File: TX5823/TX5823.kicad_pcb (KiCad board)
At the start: 2 copper layers, 84 parts, among them IC1 ATMEGA328P-A, IC2 ATTINY13A-SS, P1 Akku_in, P2 ISP, P3 Mavlink, U3 TPS7A7200RGT, U5 OPTO-TRANSISTOR4, U8 OPTO-TRANSISTOR4, Y1 16MHz

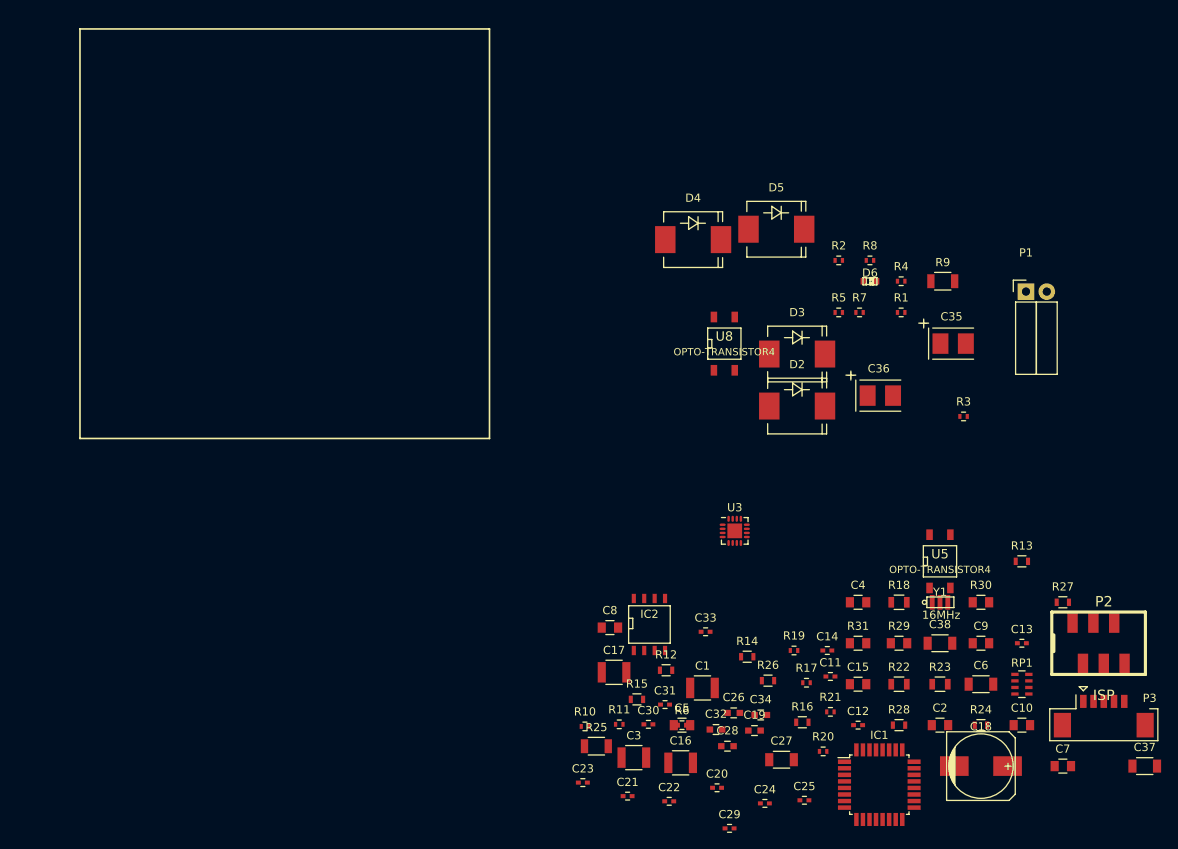
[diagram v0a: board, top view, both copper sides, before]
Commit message: weitere Footprints zugeordnet grobe Anordnung der Bauteiele im Layout
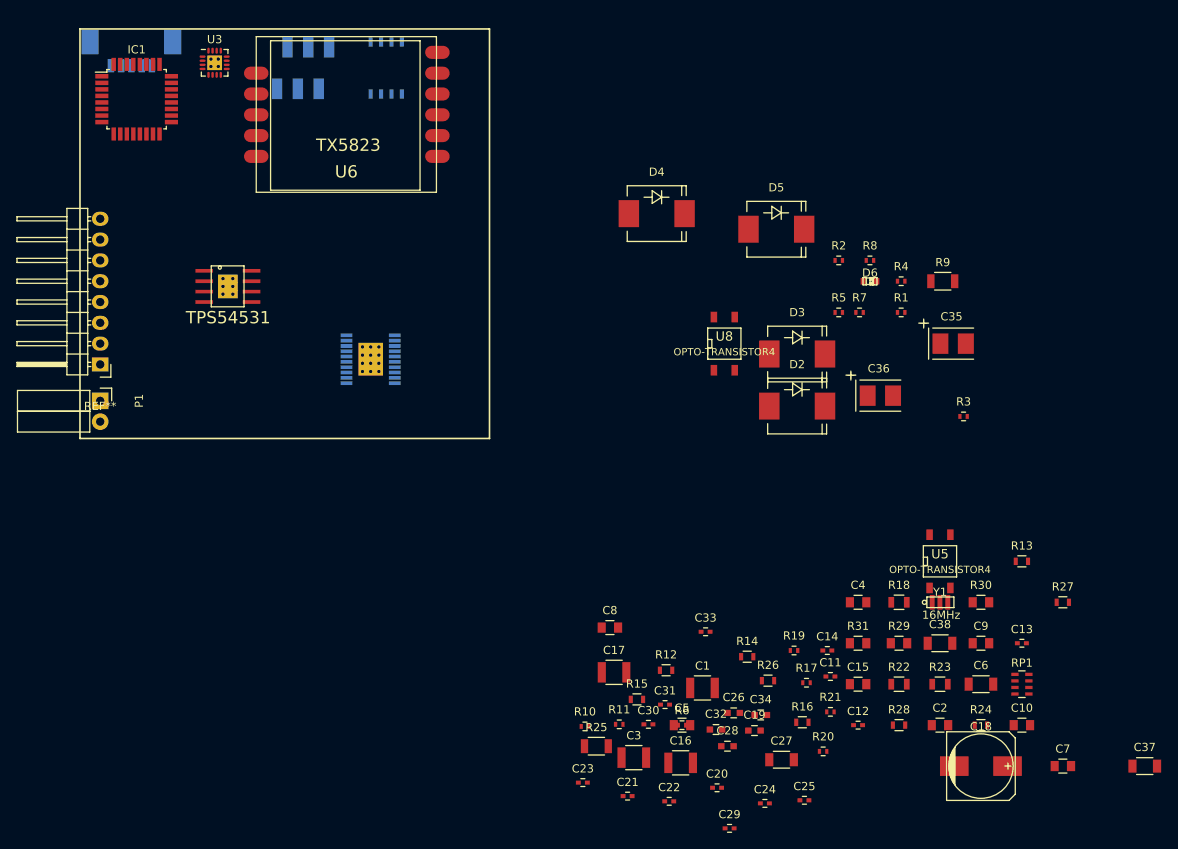
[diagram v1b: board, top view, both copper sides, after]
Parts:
- added REF**: Pin_Header_Angled_1x08, Pin_Headers:Pin_Header_Angled_1x08, F.Cu at (77.5, 61.0)
- added U1: LM25118, toni:TSSOP-20_4.4x6.5mm_Pitch0.65mm_EP, B.Cu at (110.5, 60.3)
- added U2: TPS54531, toni:SO8_EP, F.Cu at (90.2, 49.5)
- added U6: TX5823, toni:TX5823, F.Cu at (108.0, 30.5)
- IC2, P2, P3: moved to B.Cu
- U3: footprint Housings_DFN_QFN:QFN-16-1EP_3x3mm_Pitch0.5mm -> toni:QFN-16-1EP_3x3mm_Pitch0.5mm
- moved P3 145.1 mm to (81.3, 21.6)
- moved IC1 123.4 mm to (81.9, 28.6)
- moved P2 119.9 mm to (102.9, 24.8)
- moved P1 113.8 mm to (77.5, 65.4), turned to 270 degrees
- moved U3 85.4 mm to (91.4, 24.1)
- moved IC2 75.2 mm to (112.4, 24.8)
- moved D4 5.46 mm to (145.4, 42.5)
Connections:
- C11 pad 1: (no net) -> Net-(C11-Pad1)
- C12 pad 2: (no net) -> Net-(C12-Pad2)
- C13 pad 1: (no net) -> Net-(C13-Pad1)
- C14 pad 1: (no net) -> Net-(C14-Pad1)
- C14 pad 2: (no net) -> Net-(C14-Pad2)
- C15 pad 2: (no net) -> Net-(C15-Pad2)
- C2 pad 1: (no net) -> Net-(C2-Pad1)
- C4 pad 1: (no net) -> Net-(C4-Pad1)
- IC2 pad 5: (no net) -> Net-(IC2-Pad5)
- IC2 pad 7: (no net) -> Net-(IC2-Pad7)
- R3 pad 1: (no net) -> Net-(R3-Pad1)
- R4 pad 2: (no net) -> Net-(R4-Pad2)

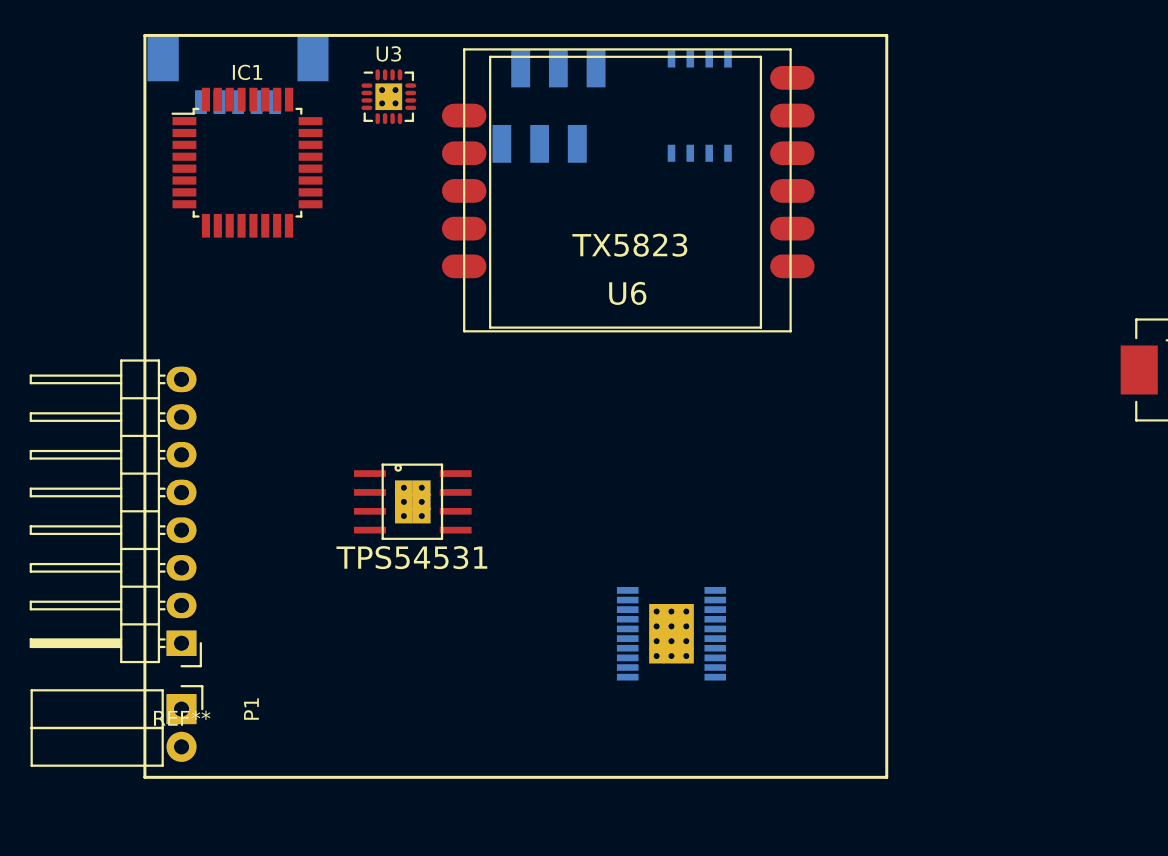
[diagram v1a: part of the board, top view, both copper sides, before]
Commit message: sma buchse hinzugefügt
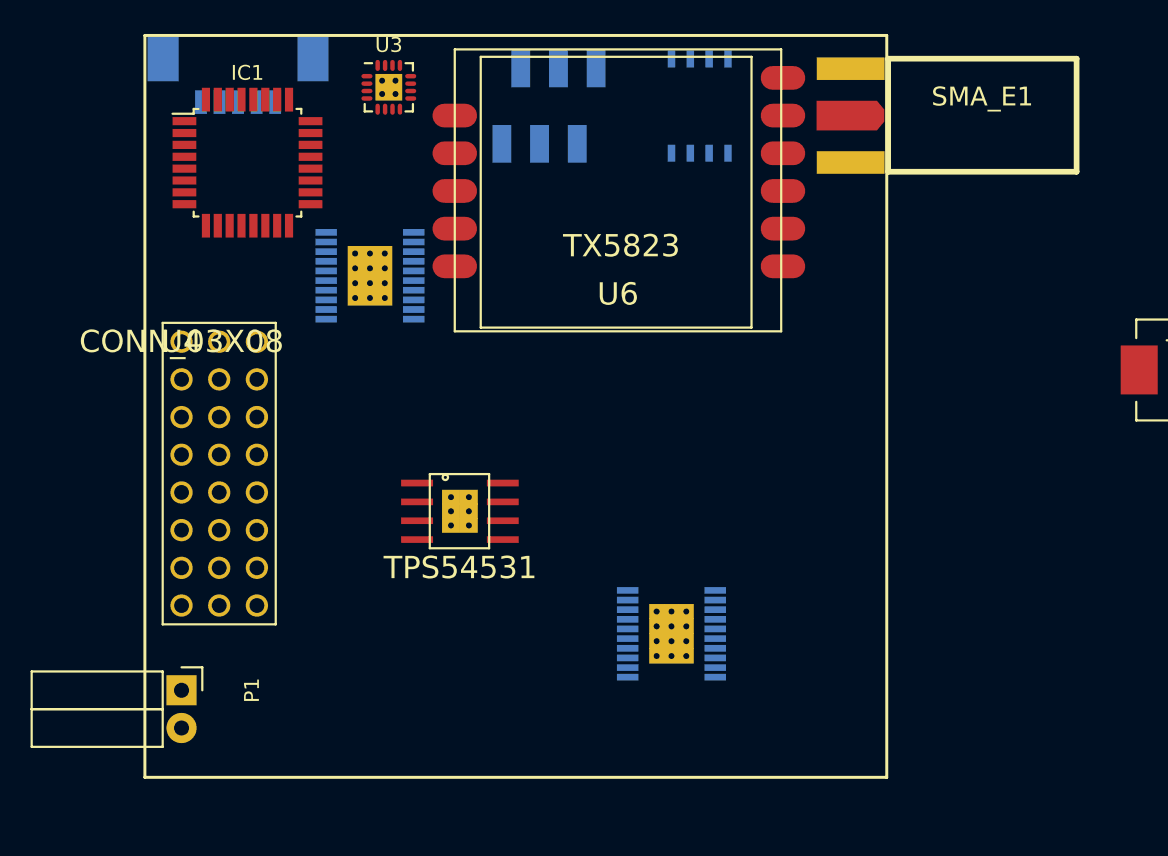
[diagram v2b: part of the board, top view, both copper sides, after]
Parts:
- removed REF**: Pin_Header_Angled_1x08, Pin_Headers:Pin_Header_Angled_1x08
- added SMA_E1: SMA_EDGE, toni:SMA_EDGE, F.Cu at (131.4, 24.1)
- added U4: CONN_03X08, toni:Conn_03x08, F.Cu at (77.5, 40.6)
- added U7: MAX7456_DS, toni:TSSOP-20_4.4x6.5mm_Pitch0.65mm_EP, B.Cu at (90.2, 36.2)
- moved U2 3.24 mm to (93.3, 50.2)
- moved P1 1.27 mm to (77.5, 64.1)
- moved U6 0.64 mm to (107.3, 30.5)
- moved U3 0.63 mm to (91.4, 23.5)
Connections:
- IC1 pad 10: (no net) -> /SSOSD-IN
- R18 pad 2: (no net) -> Net-(R18-Pad2)
- R25 pad 2: (no net) -> /IR_LED+
- RP1 pad 5: (no net) -> /HSYNC
- RP1 pad 7: (no net) -> /LOS
- U5 pad 2: (no net) -> Net-(U4-Pad7)
- U6 pad 10: (no net) -> Net-(SMA_E1-Pad1)
- U6 pad 11: (no net) -> GND
- U6 pad 2: (no net) -> /AUDIO_IN_TX

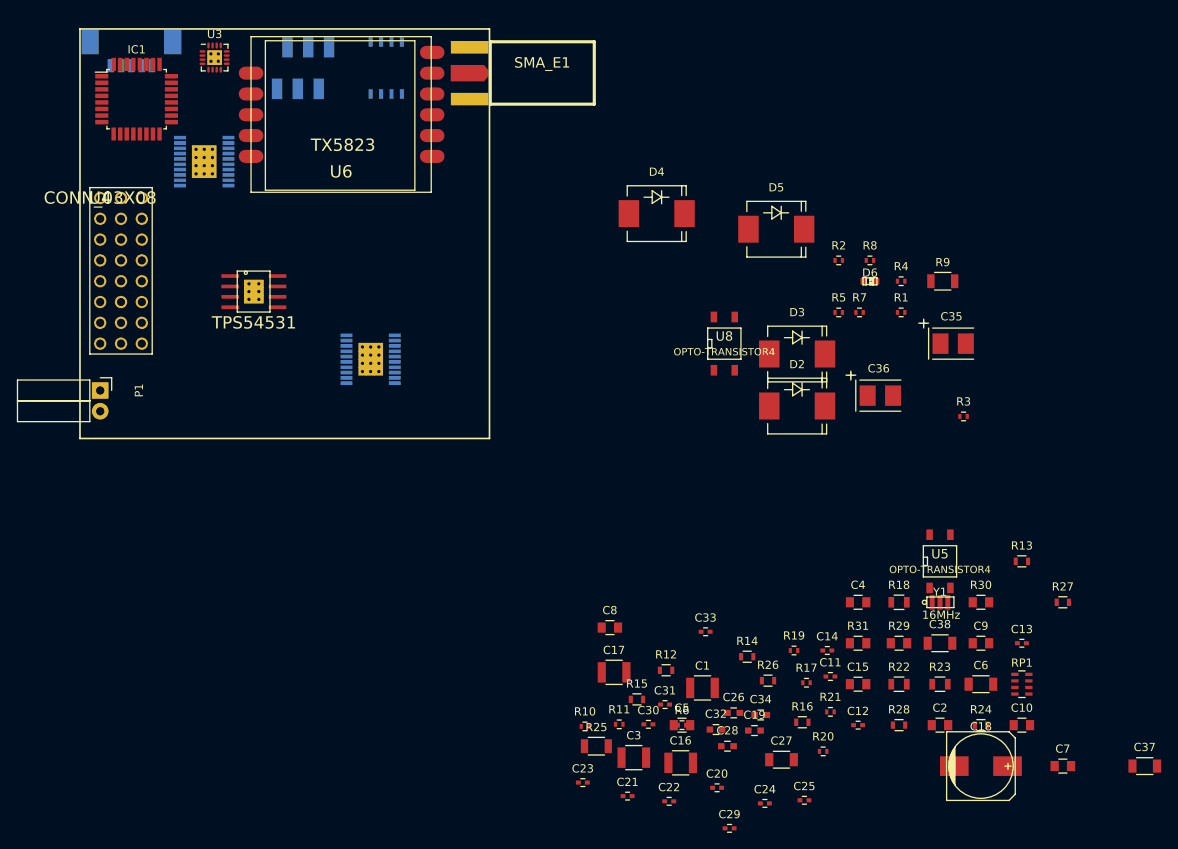
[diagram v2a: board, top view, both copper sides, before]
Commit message: Bauteile grob angeordnet
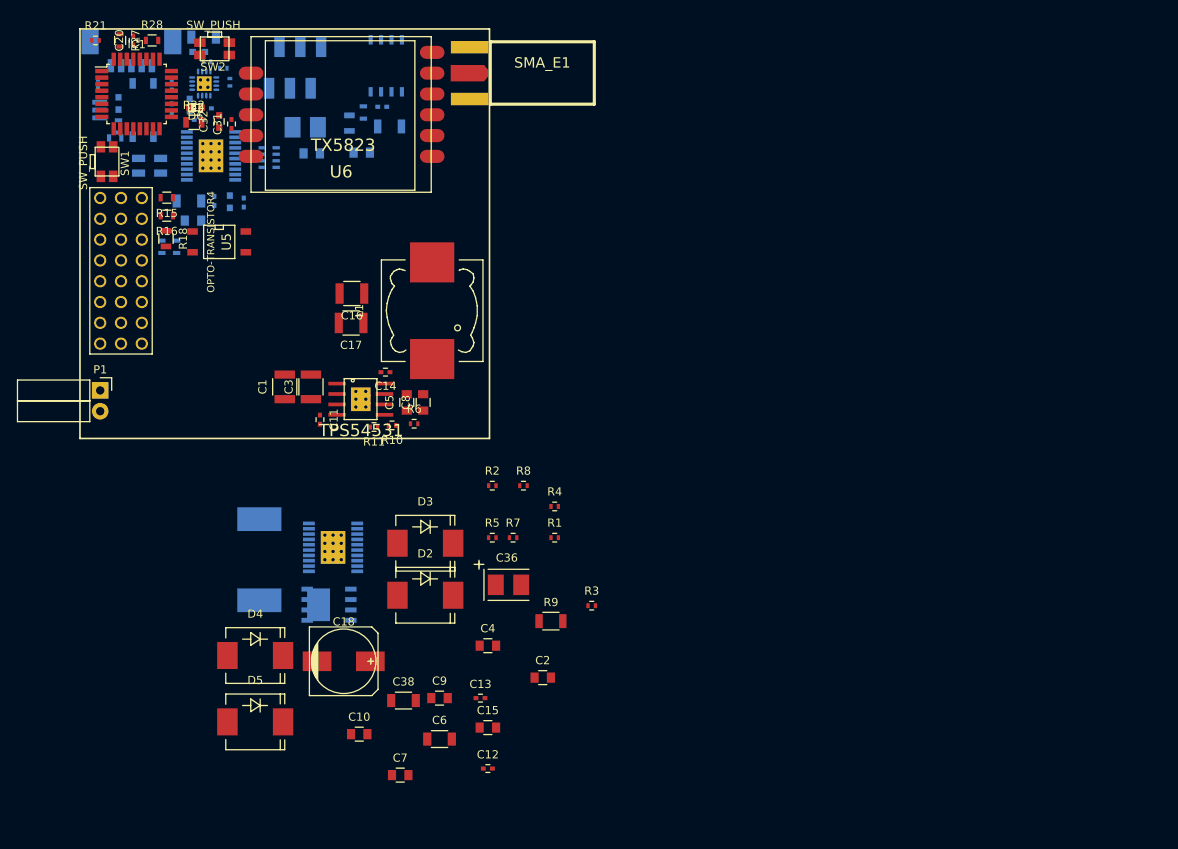
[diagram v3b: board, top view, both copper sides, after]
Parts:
- added L1: INDUCTOR, Choke_SMD:Choke_SMD_Wuerth-WE-PD-Typ-LS_Handsoldering, F.Cu at (118.0, 54.4)
- added L2: 15uH, Choke_SMD:Choke_SMD_12x12mm_h4.5mm, B.Cu at (96.9, 84.8)
- added Q1: MOS_N, toni:SO8_WITH_EP, B.Cu at (105.4, 90.3)
- added SW1: SW_PUSH, toni:EVQP7A, F.Cu at (78.1, 36.2)
- added SW2: SW_PUSH, toni:EVQP7A, F.Cu at (91.4, 22.2)
- added X1: 27MHz, toni:CRYSTAL_MT, B.Cu at (83.5, 36.7)
- C19, C21, C22, C23, C24, C25, C26, C27, C28, C29, C30, C33, C34, C35, C37, R12, R13, R14, R17, R19, R20, R23, R24, R25, R26, R29, R30, R31, RP1, U3, U8, Y1: moved to B.Cu
- moved C37 135.6 mm to (88.3, 41.0)
- moved R27 134.0 mm to (79.9, 21.4), turned to 270 degrees
- moved R28 123.7 mm to (83.8, 21.4)
- moved R13 122.4 mm to (79.7, 31.9), turned to 270 degrees
- moved R21 121.5 mm to (76.9, 21.4)
- moved C24 119.8 mm to (77.2, 26.7), turned to 90 degrees
- moved Y1 118.9 mm to (77.4, 29.9), turned to 90 degrees
- moved C20 115.8 mm to (81.5, 21.4), turned to 90 degrees
- moved C25 114.5 mm to (86.2, 29.7), turned to 90 degrees
- moved C27 113.0 mm to (90.1, 21.0)
- moved RP1 112.2 mm to (98.1, 35.7), turned to 180 degrees
- moved R22 110.1 mm to (88.9, 31.4)
- moved R20 109.2 mm to (93.3, 26.5), turned to 270 degrees
- moved C28 108.1 mm to (79.7, 29.1), turned to 90 degrees
- moved R30 106.9 mm to (88.8, 43.4)
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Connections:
- U1 pad 19: (no net) -> Net-(Q1-PadG)
- U7 pad 5: (no net) -> Net-(U7-Pad5)
- U7 pad 6: (no net) -> Net-(U7-Pad6)
